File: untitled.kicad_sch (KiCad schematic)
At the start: 64 parts, among them U1 K210_C913414, U12 PCIE-67P42H, U4 XC6206P182MR_C347373, U5 GD25LQ128EWIGR, U6 TMI7003C, U7 SGM803-TXN3/TR_C5152602, U8 XC6206P302MR_C347375, X1 X322526MMB4SI

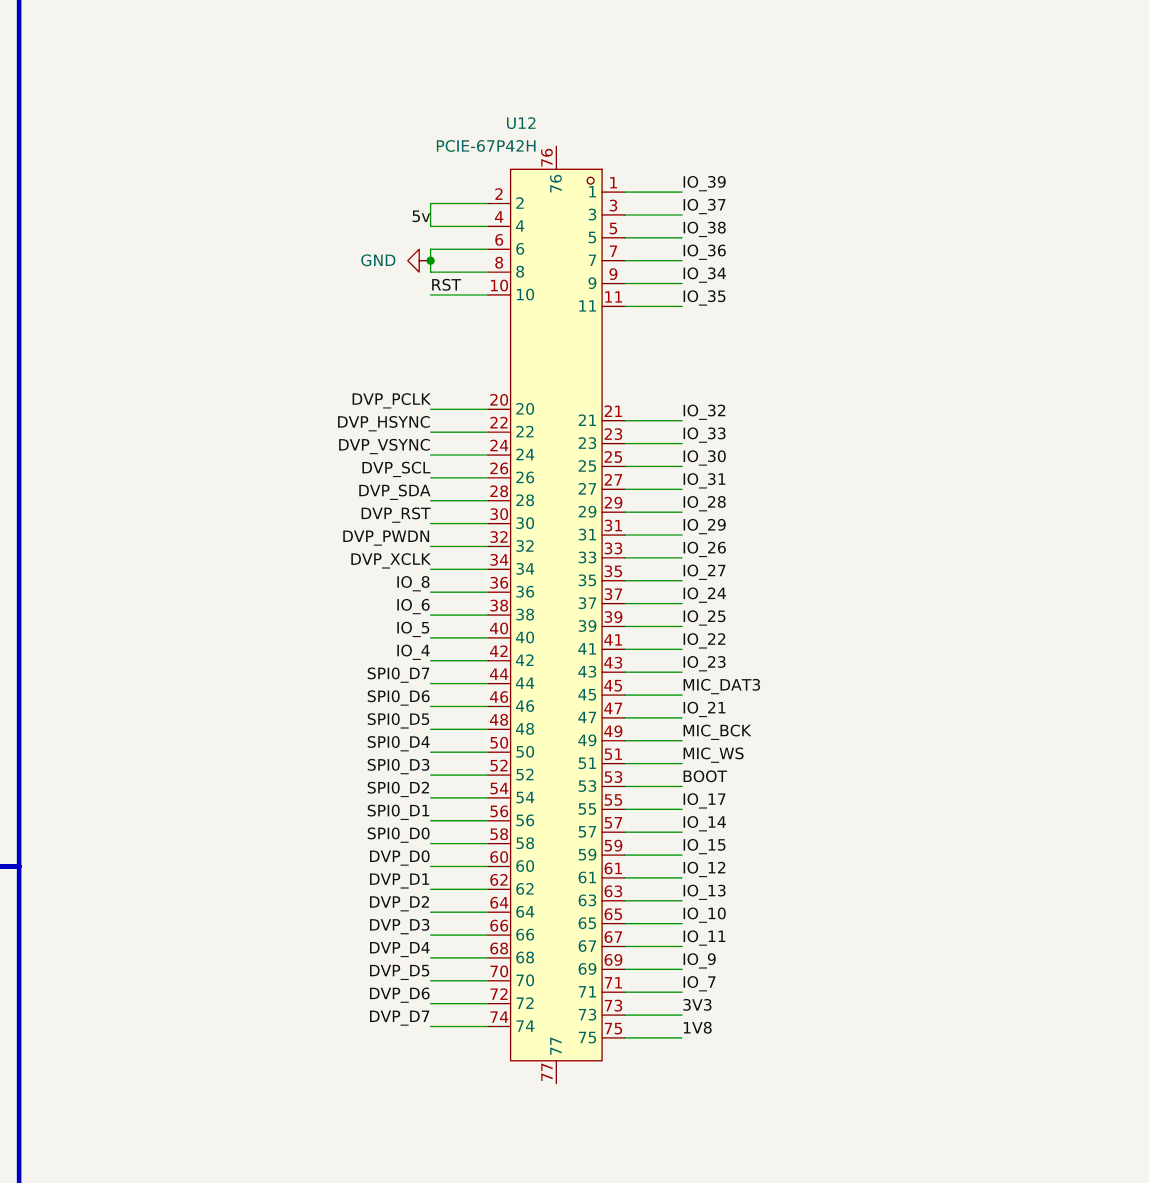
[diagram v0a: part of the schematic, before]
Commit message: detalhamento do PCIE-67P42H
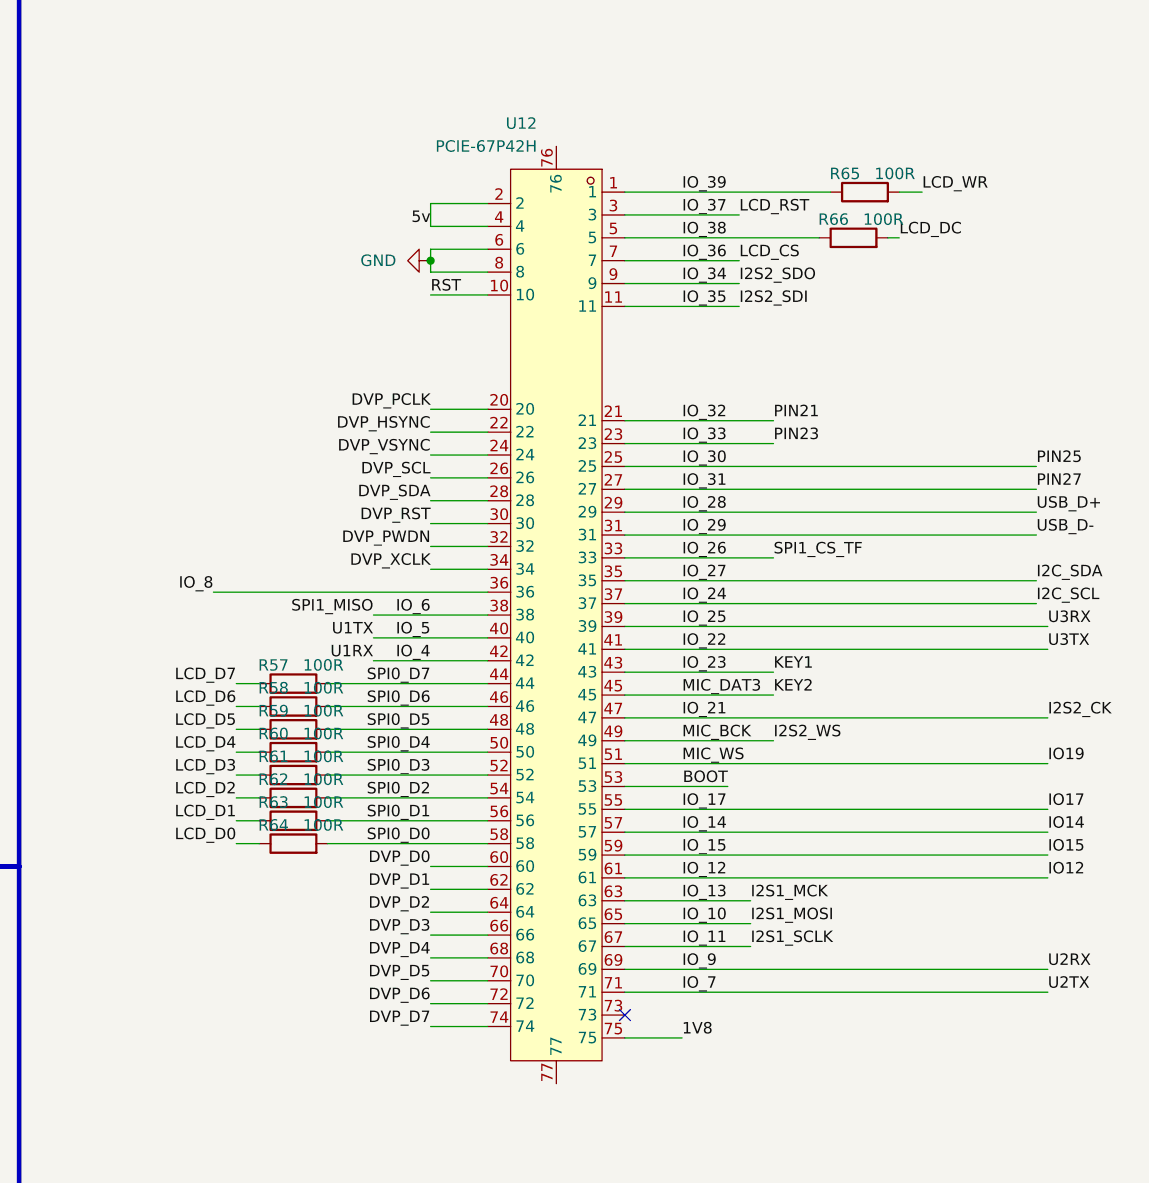
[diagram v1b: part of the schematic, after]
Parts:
- added R57, R58, R59, R60, R61, R62, R63, R64, R65, R66: 100R, Resistor_SMD:R_0201_0603Metric, symbol Device:R
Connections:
- net LCD_CS is gone; now on net IO_36: U1.A2 (IO_36)
- net LCD_RST is gone; now on net IO_37: U1.A1 (IO_37)
- net IO_38: now also R66.1
- net IO_39: now also R65.1
- net LCD_DC: now also R66.2
- net LCD_WR: now also R65.2
- net SPI0_D0: now also R64.2
- net SPI0_D1: now also R63.2
- net SPI0_D2: now also R62.2
- net SPI0_D3: now also R61.2
- net SPI0_D4: now also R60.2
- net SPI0_D5: now also R59.2
- net SPI0_D6: now also R58.2
- net SPI0_D7: now also R57.2
- net at C4.2, C5.2, C6.2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: no longer U12.73
- net IO_10 renamed I2S1_MOSI
- net IO_11 renamed I2S1_SCLK
- net IO_12 renamed IO12
- net IO_13 renamed I2S1_MCK
- net IO_14 renamed IO14
- net IO_15 renamed IO15
- net IO_17 renamed IO17
- net IO_21 renamed I2S2_CK
- net IO_24 renamed I2C_SCL
- net IO_27 renamed I2C_SDA
- net IO_34 renamed I2S2_SDO
- net IO_35 renamed I2S2_SDI
- net MIC_BCK renamed I2S2_WS
- net MIC_DAT3 renamed KEY2
- net MIC_WS renamed IO19
- new net LCD_D0: R64.1
- new net LCD_D1: R63.1
- new net LCD_D2: R62.1
- new net LCD_D3: R61.1
- new net LCD_D4: R60.1
- new net LCD_D5: R59.1
- new net LCD_D6: R58.1
- new net LCD_D7: R57.1
- no-connect marks 1 -> 2

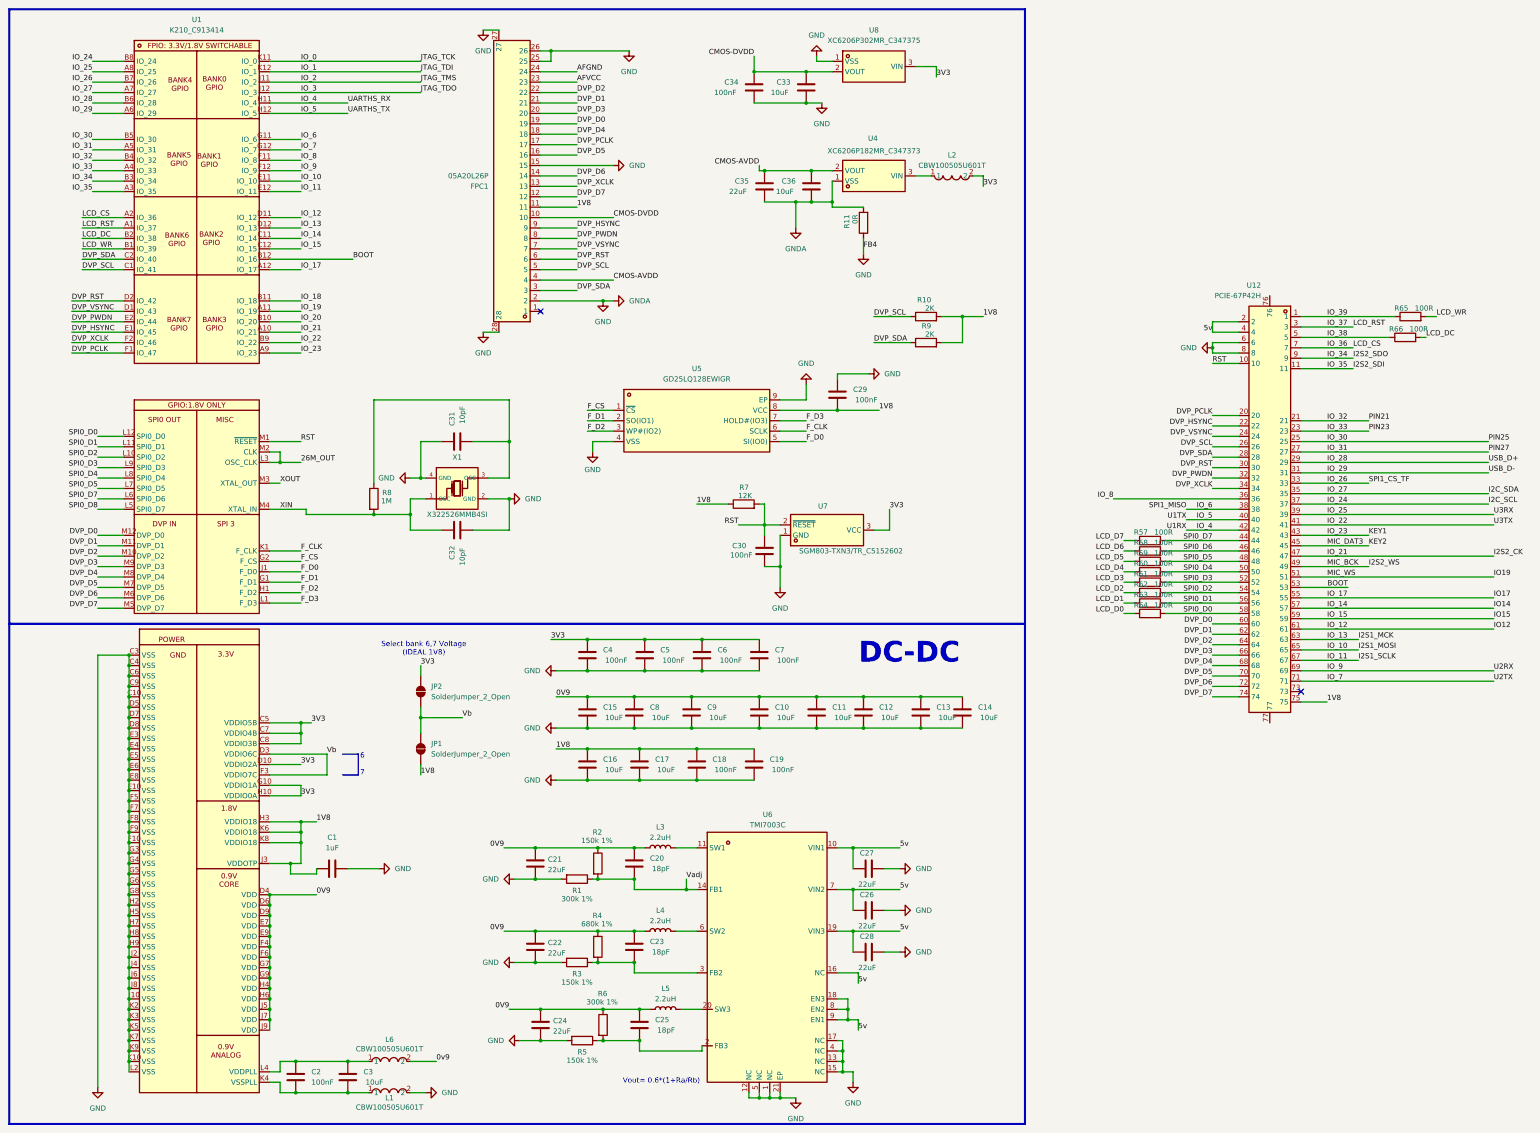
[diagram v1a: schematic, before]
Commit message: posicionamento de vias e tracos entre os componentes
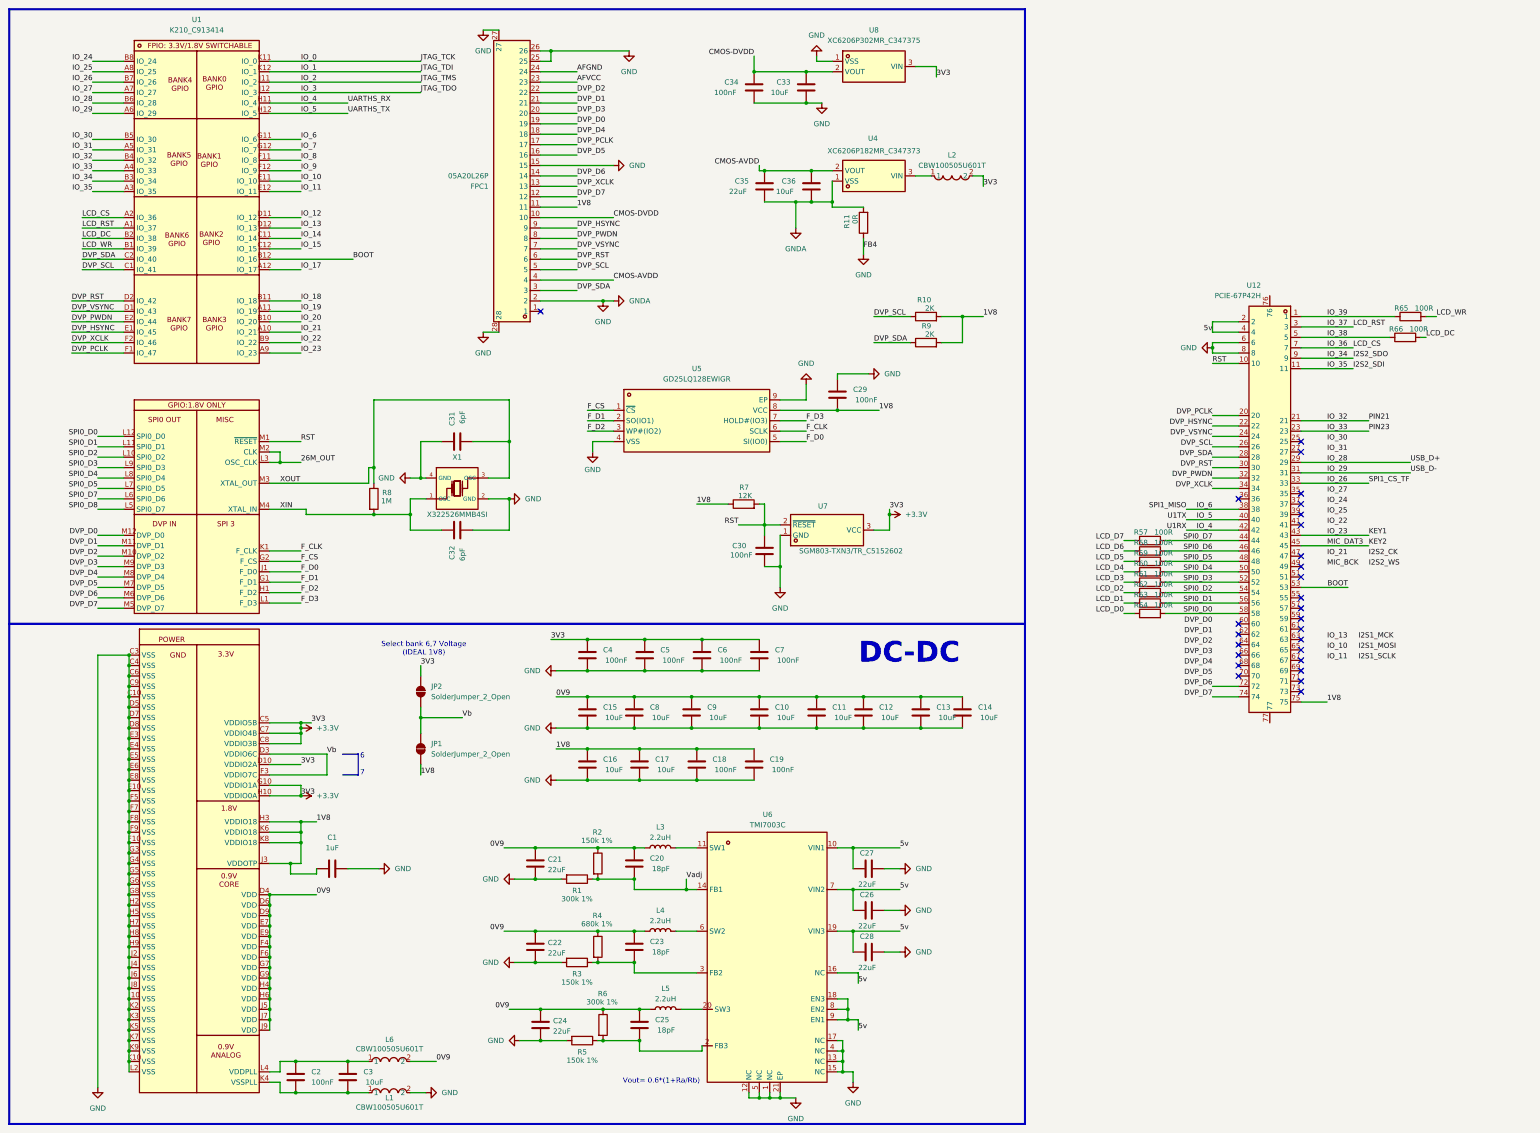
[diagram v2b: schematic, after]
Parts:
- C31, C32: value 10pF -> 6pF
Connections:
- net 0v9 is gone; now on net 0V9: L6.2
- net DVP_D0: no longer U12.60
- net DVP_D1: no longer U12.62
- net DVP_D2: no longer U12.64
- net DVP_D3: no longer U12.66
- net DVP_D4: no longer U12.68
- net DVP_D5: no longer U12.70
- net I2S1_MCK: no longer U1.D12 (IO_13), U12.63
- net I2S1_MOSI: no longer U1.E11 (IO_10), U12.65
- net I2S1_SCLK: no longer U1.E12 (IO_11), U12.67
- net I2S2_CK: no longer U1.A10 (IO_21), U12.47
- net I2S2_WS: no longer U12.49
- net IO_22: no longer U12.41
- net IO_25: no longer U12.39
- net IO_30: no longer U12.25
- net IO_31: no longer U12.27
- net IO_7: no longer U12.71
- net IO_8: no longer U12.36
- net IO_9: no longer U12.69
- net XOUT: now also C31.1, R8.1, X1.3 (OSC)
- net +3.3V: now reaches C4.2, C5.2, C6.2, C7.2, JP2.1 (A), L2.2, U1.C5 (VDDIO5B), U1.C7 (VDDIO4B), U1.C8 (VDDIO3B), U1.D10 (VDDIO2A), U1.G10 (VDDIO1A), U1.H10 (VDDIO0A), U7.3 (VCC), U8.3 (VIN)
- net at U1.K4 (VSSPLL): now also C2.1, C3.1, L1.1
- net at U1.L4 (VDDPLL): now also C2.2, C3.2, L6.1
- net I2C_SCL: no longer names the net of U12.37
- net I2C_SCL: no longer U1.B8 (IO_24)
- net I2C_SDA: no longer names the net of U12.35
- net I2C_SDA: no longer U1.A7 (IO_27)
- net IO12: no longer names the net of U12.61
- net IO12: no longer U1.D11 (IO_12)
- net IO14: no longer names the net of U12.57
- net IO14: no longer U1.C11 (IO_14)
- net IO15: no longer names the net of U12.59
- net IO15: no longer U1.C12 (IO_15)
- net IO17: no longer names the net of U12.55
- net IO17: no longer U1.A12 (IO_17)
- net IO19: no longer names the net of U12.51
- new net IO_10: U1.E11 (IO_10)
- new net IO_11: U1.E12 (IO_11)
- new net IO_12: U1.D11 (IO_12)
- new net IO_13: U1.D12 (IO_13)
- new net IO_14: U1.C11 (IO_14)
- new net IO_15: U1.C12 (IO_15)
- new net IO_17: U1.A12 (IO_17)
- new net IO_21: U1.A10 (IO_21)
- new net IO_24: U1.B8 (IO_24)
- new net IO_27: U1.A7 (IO_27)
- no-connect marks 2 -> 27
